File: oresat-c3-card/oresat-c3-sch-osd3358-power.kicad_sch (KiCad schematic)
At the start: 36 parts, among them J7 GRPB041VWVN-RC, Q6 MMBT2907, U1 OSD3358-1G-ISM, U10 SN74AUC1G07DCKR, U14 TLVH431

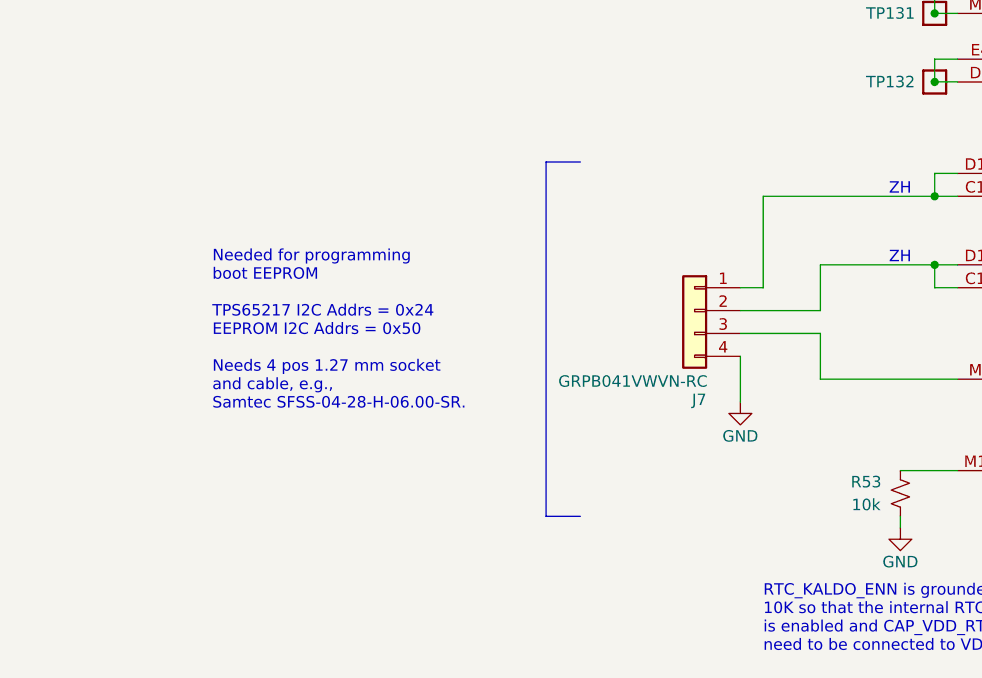
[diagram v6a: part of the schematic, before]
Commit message: Updated schematic drawing of EEPROM connector with actual labels; no substantial change
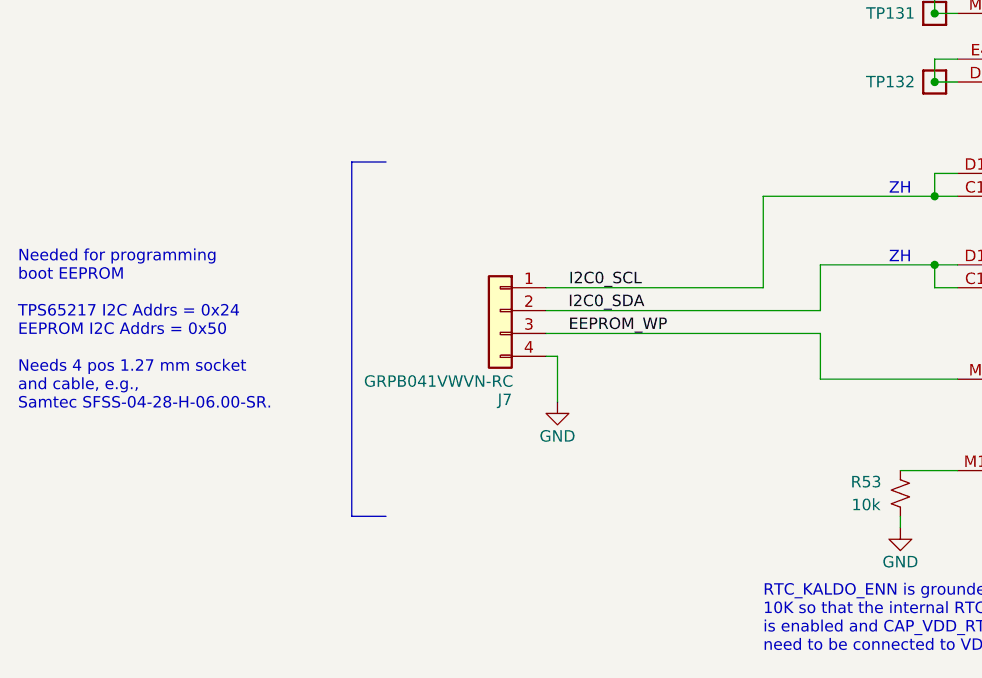
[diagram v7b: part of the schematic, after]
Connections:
- net I2C0_SCL: now reaches J7.1 (Pin_1), U1.C10 (I2C0_SCL), U1.D10 (PMIC_SCL)
- net I2C0_SDA: now reaches J7.2 (Pin_2), U1.C11 (I2C0_SDA), U1.D11 (PMIC_SDA)
- net EEPROM_WP: now reaches J7.3 (Pin_3), U1.M2 (EEPROM_WP)
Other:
- moved on the sheet: J7
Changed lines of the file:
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@@
 	(text "Needed for programming\nboot EEPROM\n\nTPS65217 I2C Addrs = 0x24\nEEPROM I2C Addrs = 0x50\n\nNeeds 4 pos 1.27 mm socket\nand cable, e.g., \nSamtec SFSS-04-28-H-06.00-SR."
 		(exclude_from_sim no)
-		(at 106.426 209.296 0)
+		(at 84.836 209.296 0)
 		(effects
 			(font
@@
 	(polyline
 		(pts
-			(xy 143.51 220.98) (xy 147.32 220.98)
+			(xy 121.92 220.98) (xy 125.73 220.98)
 		)
 		(stroke
@@
 	(polyline
 		(pts
-			(xy 147.32 181.61) (xy 143.51 181.61)
+			(xy 125.73 181.61) (xy 121.92 181.61)
 		)
 		(stroke
@@
 	(wire
 		(pts
-			(xy 165.1 200.66) (xy 173.99 200.66)
+			(xy 143.51 200.66) (xy 173.99 200.66)
 		)
 		(stroke
@@
 	(wire
 		(pts
+			(xy 144.78 203.2) (xy 144.78 208.28)
+		)
+		(stroke
+			(width 0)
+			(type default)
+		)
+	)
+	(wire
+		(pts
 			(xy 265.43 134.62) (xy 265.43 137.16)
 		)
@@
 	(polyline
 		(pts
-			(xy 143.51 181.61) (xy 143.51 220.98)
+			(xy 121.92 181.61) (xy 121.92 220.98)
 		)
 		(stroke
@@
 	(wire
 		(pts
-			(xy 165.1 203.2) (xy 165.1 208.28)
+			(xy 143.51 198.12) (xy 173.99 198.12)
 		)
 		(stroke
@@
 	(wire
 		(pts
-			(xy 165.1 198.12) (xy 173.99 198.12)
+			(xy 312.42 104.14) (xy 312.42 185.42)
 		)
 		(stroke
@@
 	(wire
 		(pts
-			(xy 312.42 104.14) (xy 312.42 185.42)
+			(xy 144.78 203.2) (xy 143.51 203.2)
 		)
 		(stroke
@@
 	(wire
 		(pts
-			(xy 167.64 195.58) (xy 165.1 195.58)
+			(xy 167.64 195.58) (xy 143.51 195.58)
 		)
 		(stroke
@@
 		)
 	)
+	(label "EEPROM_WP"
+		(at 146.0126 200.66 0)
+		(effects
+			(font
+				(size 1.27 1.27)
+			)
+			(justify left bottom)
+		)
+	)
+	(label "I2C0_SDA"
+		(at 145.9874 198.12 0)
+		(effects
+			(font
+				(size 1.27 1.27)
+			)
+			(justify left bottom)
+		)
+	)
+	(label "I2C0_SCL"
+		(at 146.05 195.58 0)
+		(effects
+			(font
+				(size 1.27 1.27)
+			)
+			(justify left bottom)
+		)
+	)
 	(global_label "VIN_USB"
 		(shape input)
@@
 	(symbol
 		(lib_id "Connector_Generic:Conn_01x04")
-		(at 160.02 198.12 0)
+		(at 138.43 198.12 0)
 		(mirror y)
 		(unit 1)
@@
 		(dnp no)
 		(property "Reference" "J7"
-			(at 160.528 208.026 0)
+			(at 138.938 208.026 0)
 			(show_name no)
 			(do_not_autoplace no)
@@
 		)
 		(property "Value" "GRPB041VWVN-RC"
-			(at 153.162 205.994 0)
+			(at 131.572 205.994 0)
 			(show_name no)
 			(do_not_autoplace no)
@@
 		)
 		(property "Footprint" "Connector_PinHeader_1.27mm:PinHeader_1x04_P1.27mm_Vertical"
-			(at 160.02 198.12 0)
+			(at 138.43 198.12 0)
 			(hide yes)
 			(show_name no)
@@
 		)
 		(property "Datasheet" "https://s3.amazonaws.com/catalogspreads-pdf/PAGE94-95%20.050%20MALE%20HDR%20ST%20RA%20SMT.pdf"
-			(at 160.02 198.12 0)
+			(at 138.43 198.12 0)
 			(hide yes)
 			(show_name no)
@@
 		)
 		(property "Description" "Connector Header Through Hole 4 position 0.050\" (1.27mm)"
-			(at 160.02 198.12 0)
+			(at 138.43 198.12 0)
 			(hide yes)
 			(show_name no)
@@
 		)
 		(property "DPN" "S9014E-04-ND"
-			(at 160.02 198.12 0)
+			(at 138.43 198.12 0)
 			(hide yes)
 			(show_name no)
@@
 		)
 		(property "DST" "DigiKey"
-			(at 160.02 198.12 0)
+			(at 138.43 198.12 0)
 			(hide yes)
 			(show_name no)
@@
 		)
 		(property "MFR" "Sullins Connector Solutions"
-			(at 160.02 198.12 0)
+			(at 138.43 198.12 0)
 			(hide yes)
 			(show_name no)
@@
 		)
 		(property "MPN" "GRPB041VWVN-RC"
-			(at 160.02 198.12 0)
+			(at 138.43 198.12 0)
 			(hide yes)
 			(show_name no)
@@
 	(symbol
 		(lib_id "power:GND")
-		(at 165.1 208.28 0)
+		(at 144.78 208.28 0)
 		(unit 1)
 		(body_style 1)
@@
 		(dnp no)
 		(property "Reference" "#PWR0145"
-			(at 165.1 214.63 0)
+			(at 144.78 214.63 0)
 			(hide yes)
 			(show_name no)
@@
 		)
 		(property "Value" "GND"
-			(at 165.1 212.09 0)
+			(at 144.78 212.09 0)
 			(show_name no)
 			(do_not_autoplace no)
@@
 		)
 		(property "Footprint" ""
-			(at 165.1 208.28 0)
+			(at 144.78 208.28 0)
 			(hide yes)
 			(show_name no)
@@
 		)
 		(property "Datasheet" ""
-			(at 165.1 208.28 0)
+			(at 144.78 208.28 0)
 			(hide yes)
 			(show_name no)
@@
 		)
 		(property "Description" "Power symbol creates a global label with name \"GND\" , ground"
-			(at 165.1 208.28 0)
+			(at 144.78 208.28 0)
 			(hide yes)
 			(show_name no)
